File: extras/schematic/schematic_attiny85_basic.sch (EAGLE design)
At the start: 21 parts, among them SW1 Seek Down, SW2 Seek Up, U1 SI4735-D60-GU, U2 ATTINY85-P

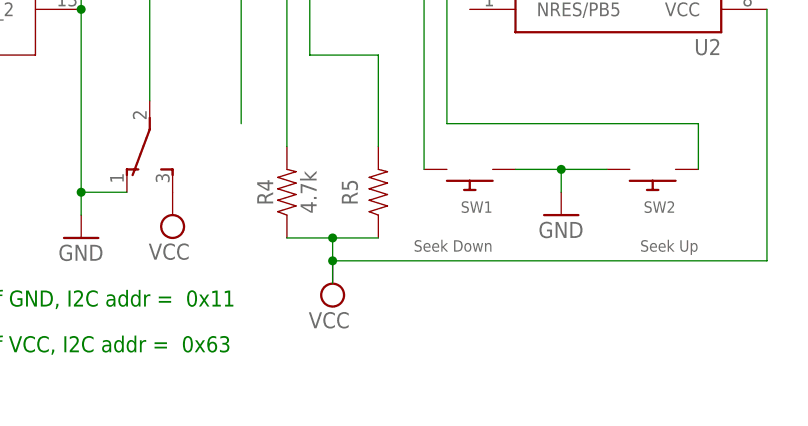
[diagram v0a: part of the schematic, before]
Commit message: SI473X Arduino Library
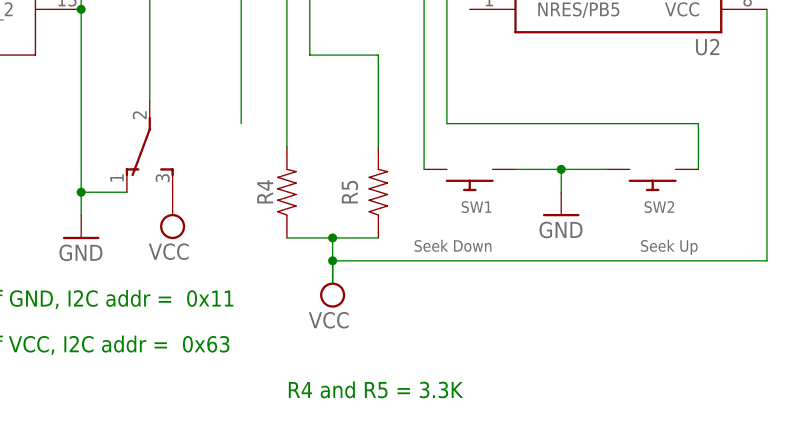
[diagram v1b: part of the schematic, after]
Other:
- note added: "R4 and R5 = 3.3K"
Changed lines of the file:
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@@
 <text x="22.86" y="55.88" size="1.778" layer="91">If GND, I2C addr =  0x11</text>
 <text x="22.86" y="50.8" size="1.778" layer="91">If VCC, I2C addr =  0x63</text>
+<text x="55.88" y="45.72" size="1.778" layer="91">R4 and R5 = 3.3K</text>
 </plain>
 <instances>
@@
 <instance part="R4" gate="G$1" x="55.88" y="68.58" smashed="yes" rot="R90">
 <attribute name="NAME" x="54.356" y="68.58" size="1.778" layer="95" font="vector" rot="R90" align="bottom-center"/>
-<attribute name="VALUE" x="57.404" y="68.58" size="1.778" layer="96" font="vector" rot="R90" align="top-center"/>
 </instance>
 <instance part="R5" gate="G$1" x="66.04" y="68.58" smashed="yes" rot="R90">
